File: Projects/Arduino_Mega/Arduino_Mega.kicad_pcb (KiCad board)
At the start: 2 copper layers, 101.6 x 53.3 mm, 13 parts, among them J1 Power, J2 PWM, J3 Analog, J4 PWM, J5 Analog, J6 Communication, J7 Digital

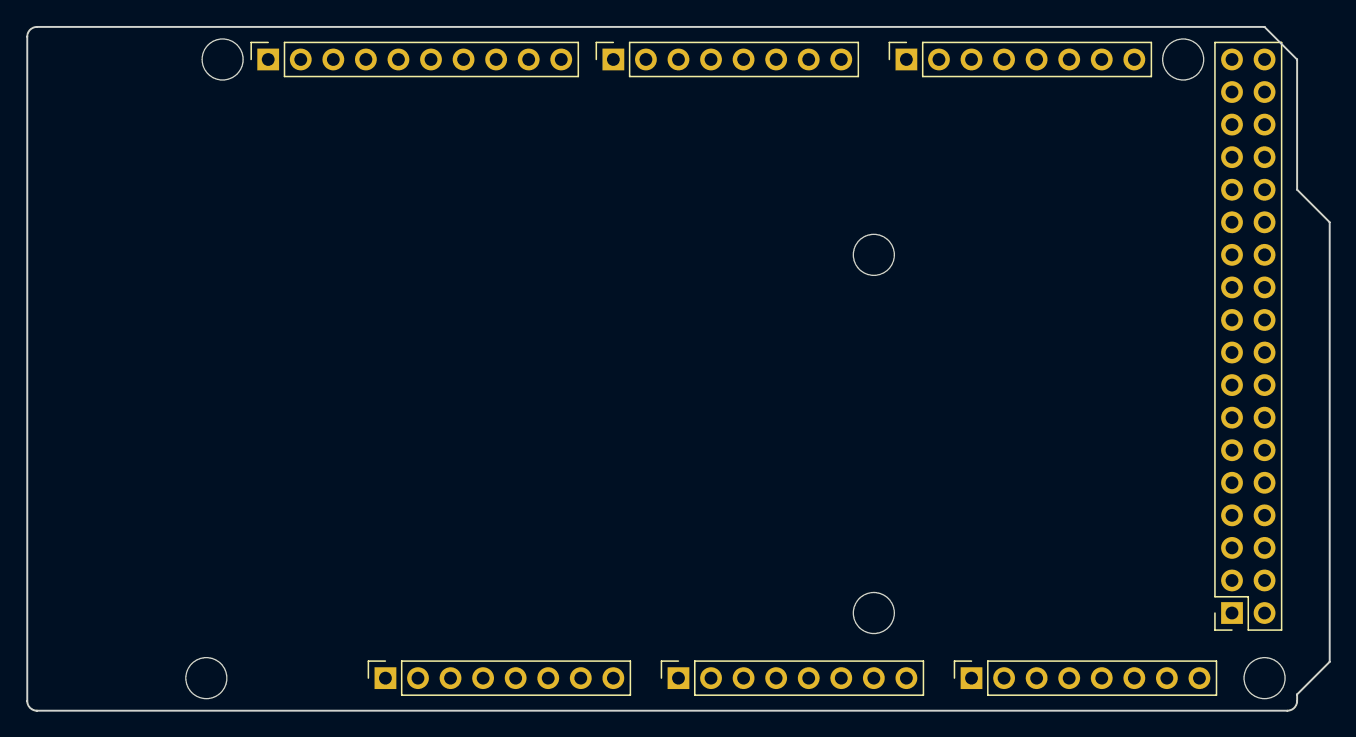
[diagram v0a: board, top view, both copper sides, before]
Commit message: adding parts placer position file to arduino mega
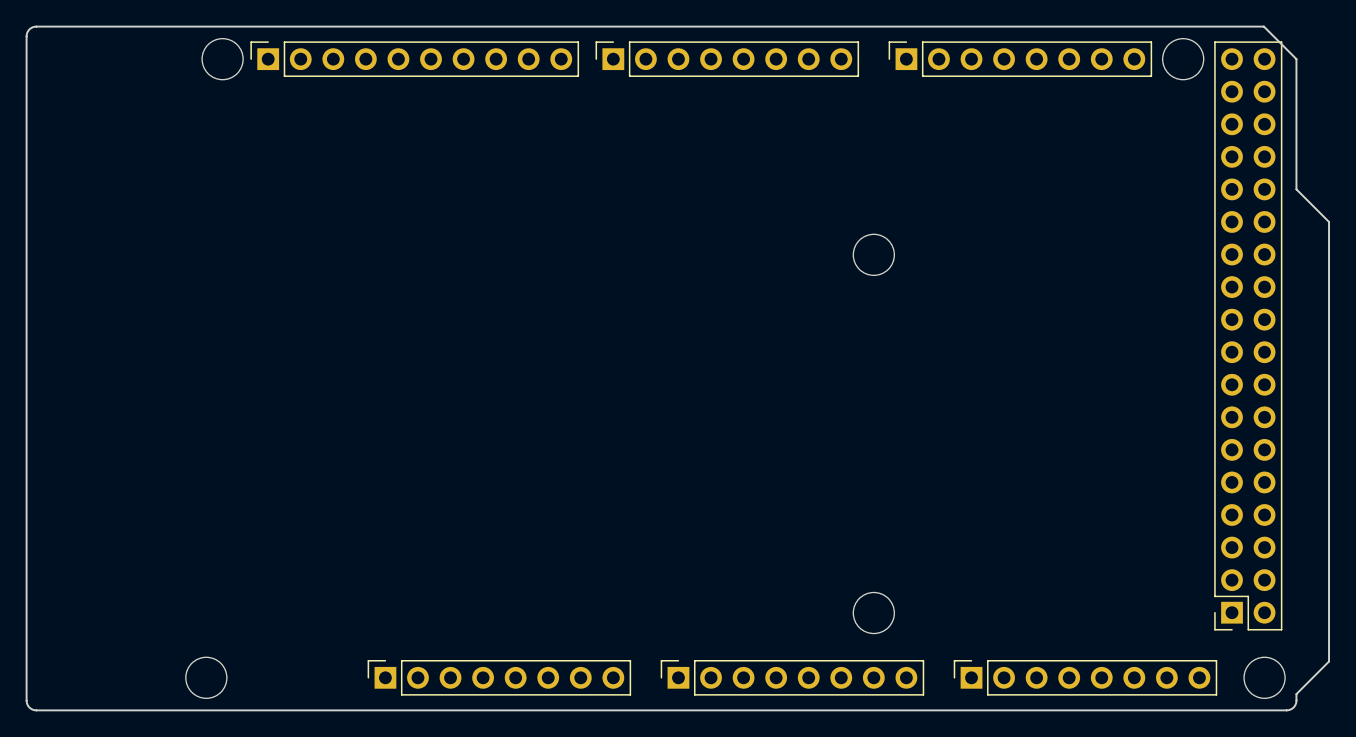
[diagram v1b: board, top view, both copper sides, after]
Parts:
- added BOARD: board, Library:board, F.Cu at (150.7, 73.3)
